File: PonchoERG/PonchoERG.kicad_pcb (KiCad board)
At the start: 2 copper layers, 86.4 x 96.5 mm, 66 parts, among them J1 Entradas Analógicas, J2 I/O's Multi Propósito, J3 POWER_PONCHO, J4 CONN_02X04, U1 TPD4E1B06, U2 TPD4E1B06, U3 TPD4E1B06, U4 TPD4E1B06, U5 TPD4E1B06, U6 ADS1299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

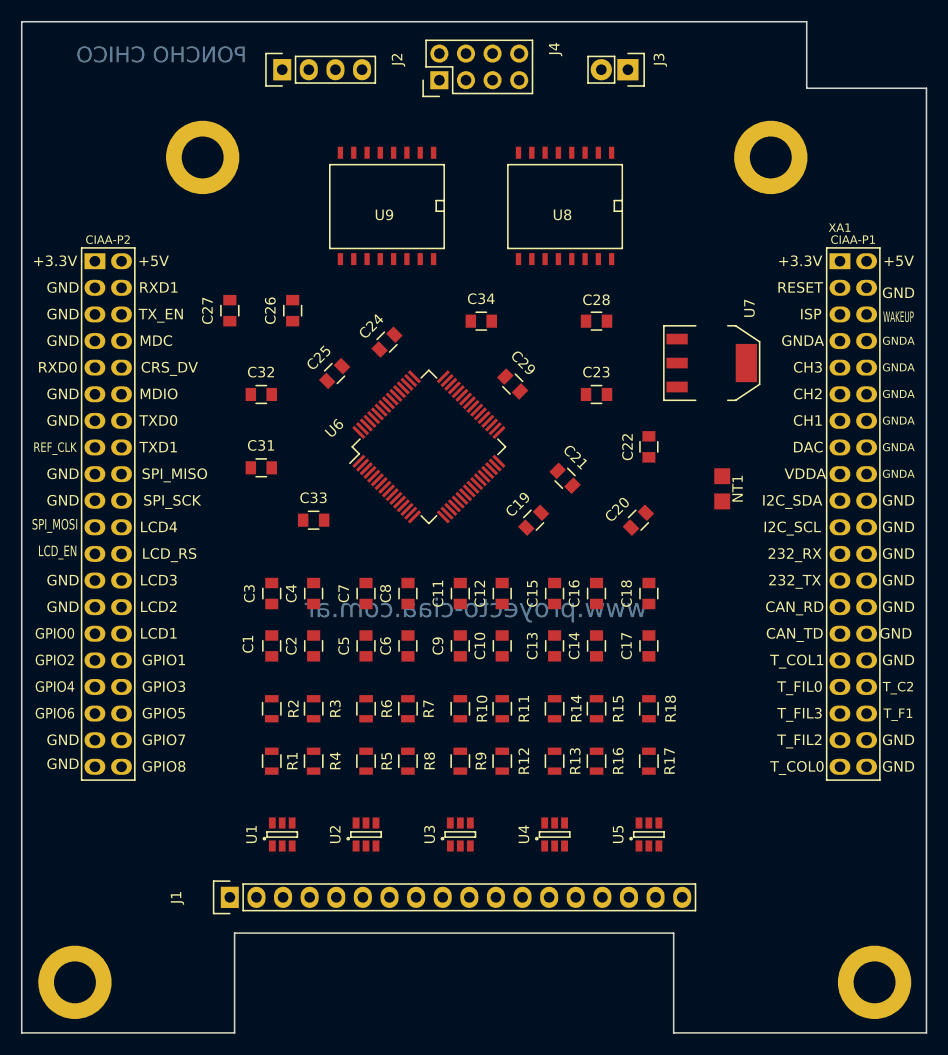
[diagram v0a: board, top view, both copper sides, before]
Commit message: Actualización 1.0 - Inclusión de nuevos diodos de protección TPD2E001. - Creación de librería TPD2E001 y rediseño de esquemático. - Reubicación de componentes.
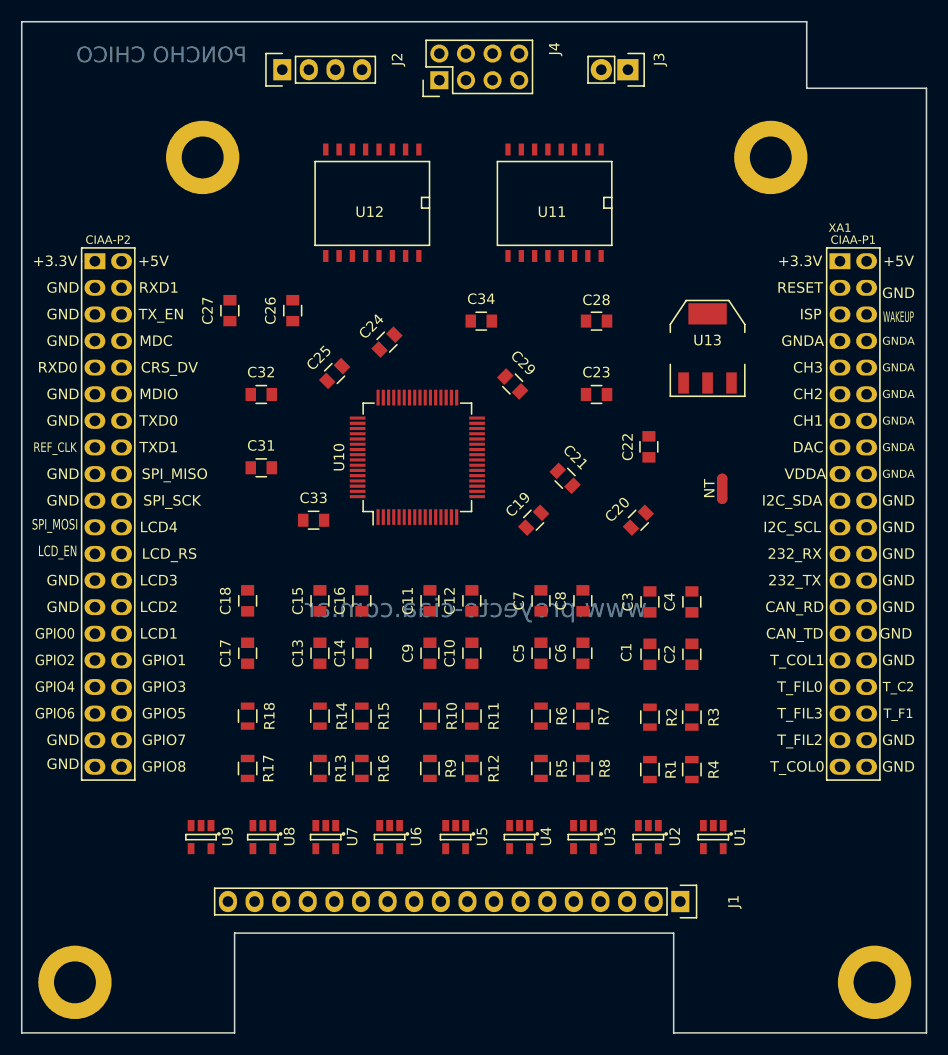
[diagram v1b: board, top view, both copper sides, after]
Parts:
- added U10: ADS1299, Housings_QFP:TQFP-64_10x10mm_Pitch0.5mm, F.Cu at (138.9, 85.0)
- added U11: ADuM6401, SMD_Packages:SO-16-W, F.Cu at (152.0, 60.7)
- added U12: ADuM2401, SMD_Packages:SO-16-W, F.Cu at (134.6, 60.7)
- added U13: NCP1117ST33T3G, TO_SOT_Packages_SMD:SOT-223, F.Cu at (166.6, 74.6)
- NT1: footprint Otros:NT -> OtrosFoot:NET-TIE-1mm
- U1, U2, U3, U4, U5: value TPD4E1B06 -> TPD2E001; footprint TO_SOT_Packages_SMD:SOT-23-6 -> TO_SOT_Packages_SMD:SOT-23-5
- U6: value ADS1299 -> TPD2E001; footprint Housings_QFP:TQFP-64_10x10mm_Pitch0.5mm -> TO_SOT_Packages_SMD:SOT-23-5
- U7: value NCP1117ST33T3G -> TPD2E001; footprint TO_SOT_Packages_SMD:SOT-223 -> TO_SOT_Packages_SMD:SOT-23-5
- U8: value ADuM6401 -> TPD2E001; footprint SMD_Packages:SO-16-W -> TO_SOT_Packages_SMD:SOT-23-5
- U9: value ADuM2401 -> TPD2E001; footprint SMD_Packages:SO-16-W -> TO_SOT_Packages_SMD:SOT-23-5
- moved U8 66.8 mm to (124.2, 121.2), turned to 270 degrees
- moved U9 62.8 mm to (118.2, 121.2), turned to 270 degrees
- moved U7 58.4 mm to (130.2, 121.2)
- moved J1 43.0 mm to (164.0, 127.4), turned to 270 degrees
- moved U1 41.2 mm to (167.2, 121.2), turned to 270 degrees
- moved C17 38.3 mm to (122.7, 103.7)
- moved C18 38.3 mm to (122.7, 98.7)
- moved R17 38.3 mm to (122.7, 114.7)
- moved R18 38.3 mm to (122.7, 109.7)
- moved U6 37.4 mm to (136.2, 121.2), turned to 270 degrees
- moved C1 36.1 mm to (161.1, 103.8)
- moved C2 36.1 mm to (165.1, 103.8)
- moved C3 36.1 mm to (161.1, 98.8)
- moved C4 36.1 mm to (165.1, 98.8)
- moved R1 36.1 mm to (161.1, 114.8)
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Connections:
- U1 pad 1: Net-(J1-Pad1) -> +3V3
- U1 pad 2: Net-(J1-Pad2) -> (no net)
- U1 pad 3: GNDD -> Net-(J1-Pad1)
- U1 pad 4: Net-(J1-Pad3) -> GNDD
- U1 pad 5: Net-(J1-Pad4) -> Net-(J1-Pad2)
- U2 pad 1: Net-(J1-Pad5) -> +3V3
- U2 pad 2: Net-(J1-Pad6) -> (no net)
- U2 pad 3: GNDD -> Net-(J1-Pad3)
- U2 pad 4: Net-(J1-Pad7) -> GNDD
- U2 pad 5: Net-(J1-Pad8) -> Net-(J1-Pad4)
- U3 pad 1: Net-(J1-Pad9) -> +3V3
- U3 pad 2: Net-(J1-Pad10) -> (no net)
- U3 pad 3: GNDD -> Net-(J1-Pad5)
- U3 pad 4: Net-(J1-Pad11) -> GNDD
- U3 pad 5: Net-(J1-Pad12) -> Net-(J1-Pad6)
- U4 pad 1: Net-(J1-Pad13) -> +3V3
- U4 pad 2: Net-(J1-Pad14) -> (no net)
- U4 pad 3: GNDD -> Net-(J1-Pad7)
- U4 pad 4: Net-(J1-Pad15) -> GNDD
- U4 pad 5: Net-(J1-Pad16) -> Net-(J1-Pad8)
- U5 pad 1: Net-(J1-Pad17) -> +3V3
- U5 pad 2: Net-(J1-Pad18) -> (no net)
- U5 pad 3: GNDD -> Net-(J1-Pad9)
- U5 pad 4: (no net) -> GNDD
- U5 pad 5: (no net) -> Net-(J1-Pad10)
- U6 pad 1: /ADS1299/IN8- -> +3V3
- U6 pad 2: /ADS1299/IN8+ -> (no net)
- U6 pad 3: /ADS1299/IN7- -> Net-(J1-Pad11)
- U6 pad 4: /ADS1299/IN7+ -> GNDD
- U6 pad 5: /ADS1299/IN6- -> Net-(J1-Pad12)
- U7 pad 1: GNDA -> +3V3
- U7 pad 2: +3V3 -> (no net)
- U7 pad 3: +5VA -> Net-(J1-Pad13)
- U7 pad 4: (no net) -> GNDD
- U8 pad 1: Net-(J3-Pad1) -> +3V3
- U8 pad 2: Net-(J3-Pad2) -> (no net)
- U8 pad 3: /AISLACIÓN/CS1/ -> Net-(J1-Pad15)
- U8 pad 4: /AISLACIÓN/SCLK1 -> GNDD
- U8 pad 5: /AISLACIÓN/MOSI1 -> Net-(J1-Pad16)
- U9 pad 1: Net-(J3-Pad1) -> +3V3
- U9 pad 2: Net-(J3-Pad2) -> (no net)
- U9 pad 3: /AISLACIÓN/START1 -> Net-(J1-Pad17)
- U9 pad 4: /AISLACIÓN/RESET1 -> GNDD
- U9 pad 5: (no net) -> Net-(J1-Pad18)

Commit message: Reubicación de ADS y componentes pasivos asociados. Sujeto a revisión.
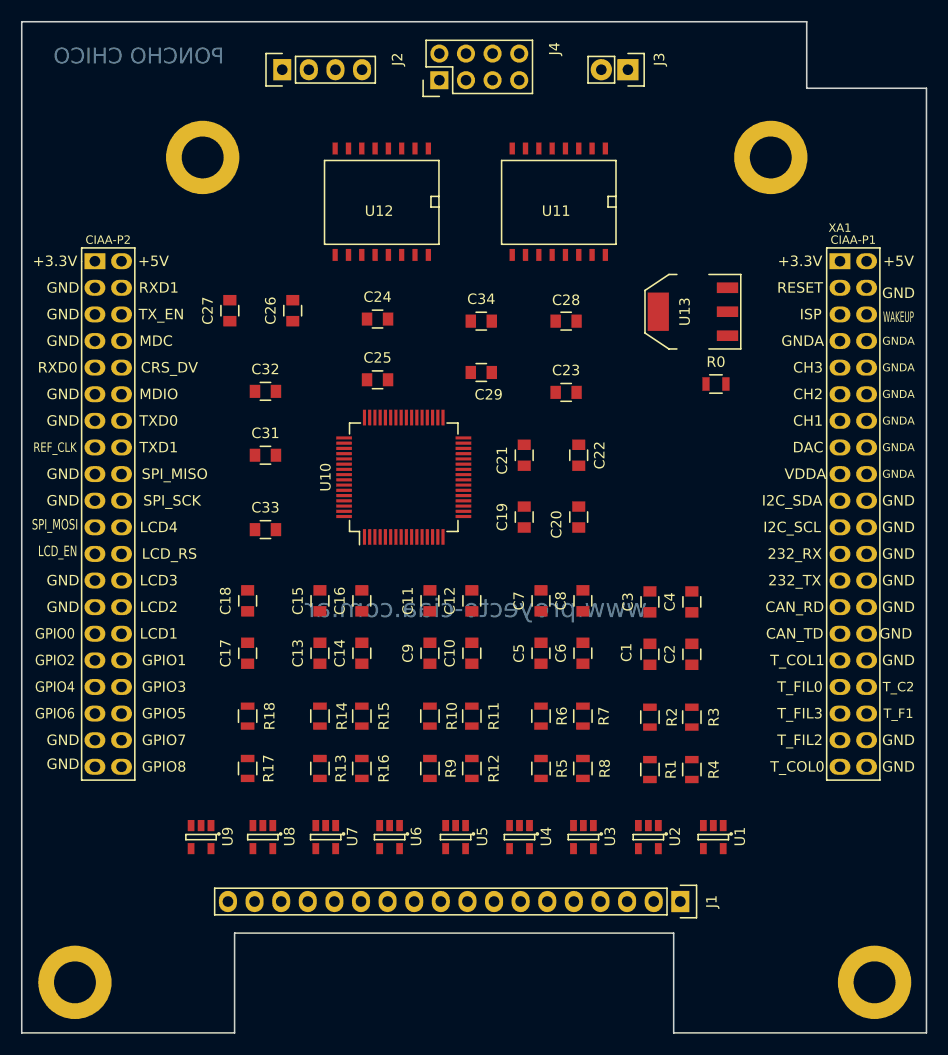
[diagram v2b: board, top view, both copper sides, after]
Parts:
- removed NT1: Net_Tie, OtrosFoot:NET-TIE-1mm
- added R0: 0, Resistors_SMD:R_0805, F.Cu at (167.4, 78.0)
- moved C22 6.75 mm to (154.3, 84.8), turned to 270 degrees
- moved C20 5.71 mm to (154.3, 90.7), turned to 90 degrees
- moved C33 4.69 mm to (124.4, 91.9)
- moved C21 4.48 mm to (149.1, 84.8), turned to 270 degrees
- moved C25 4.14 mm to (135.1, 77.6), turned to 0 degrees
- moved U13 3.77 mm to (165.2, 71.1), turned to 90 degrees
- moved C29 3.20 mm to (145.0, 76.9), turned to 0 degrees
- moved C23 2.91 mm to (153.1, 78.8)
- moved C28 2.90 mm to (153.1, 72.0)
- moved C24 2.38 mm to (135.1, 71.8), turned to 0 degrees
- moved U10 2.30 mm to (137.6, 86.9)
- moved C31 1.26 mm to (124.4, 84.8)
- moved C19 0.95 mm to (149.1, 90.7), turned to 90 degrees
- moved U12 0.91 mm to (135.5, 60.6)
- moved C32 0.50 mm to (124.4, 78.7)
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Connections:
- C26 pad 1: +5VA -> +3.3V
- C26 pad 2: GNDA -> GNDD
- C27 pad 1: +5VA -> +3.3V
- C27 pad 2: GNDA -> GNDD
- C28 pad 1: +3V3 -> +5V
- C28 pad 2: GNDD -> GNDA
- C29 pad 1: +3V3 -> +5V
- C29 pad 2: GNDD -> GNDA
- C31 pad 1: +5VA -> +5V
- C32 pad 1: +5VA -> +5V
- C33 pad 1: +5VA -> +5V
- C34 pad 1: +3V3 -> +3.3V
- U1 pad 1: +3V3 -> +3.3V
- U10 pad 19: +5VA -> +3.3V
- U10 pad 21: +5VA -> +3.3V
- U10 pad 22: +5VA -> +3.3V
- U10 pad 35: +3V3 -> +3.3V
- U10 pad 48: +3V3 -> +3.3V
- U10 pad 50: +3V3 -> +3.3V
- U10 pad 52: +3V3 -> +3.3V
- U10 pad 54: +5VA -> +3.3V
- U10 pad 56: +5VA -> +3.3V
- U10 pad 59: +5VA -> +3.3V
- U11 pad 10: +5VA -> +5V
- U11 pad 16: +5VA -> +5V
- U12 pad 10: +5VA -> +5V
- U12 pad 16: +5VA -> +5V
- U13 pad 2: +3V3 -> +3.3V
- U13 pad 3: +5VA -> +5V
- U2 pad 1: +3V3 -> +3.3V
- U3 pad 1: +3V3 -> +3.3V
- U4 pad 1: +3V3 -> +3.3V
- U5 pad 1: +3V3 -> +3.3V
- U6 pad 1: +3V3 -> +3.3V
- U7 pad 1: +3V3 -> +3.3V
- U8 pad 1: +3V3 -> +3.3V
- U9 pad 1: +3V3 -> +3.3V
